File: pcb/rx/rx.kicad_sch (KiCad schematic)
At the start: 2 parts, among them U1 MCP33151-05-E/MS, U2 NCS20162DR2G

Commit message: Backup Prototype
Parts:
- removed U1: MCP33151-05-E/MS, custom-lib:MCP33151-05-E_MS, symbol library:MCP33151-05-E/MS
- removed U2: NCS20162DR2G, custom-lib:NCS20162, symbol library:NCS20162DR2G
- added C1: 33nF, Capacitor_THT:C_Disc_D5.0mm_W2.5mm_P5.00mm, symbol Device:C_Small
- added C10, C12, C17, C19, C3, C6: 330pF, Capacitor_THT:C_Disc_D5.0mm_W2.5mm_P5.00mm, symbol Device:C_Small
- added C11, C18, C26, C27, C29, C4: 0.1uF, Capacitor_THT:C_Disc_D5.0mm_W2.5mm_P5.00mm, symbol Device:C_Small
- added C13, C20, C5: 100nF, Capacitor_THT:C_Disc_D5.0mm_W2.5mm_P5.00mm, symbol Device:C_Small
- added C14, C21, C7: 1nF, Capacitor_THT:C_Disc_D5.0mm_W2.5mm_P5.00mm, symbol Device:C_Small
- added C15, C8: 10nF, Capacitor_THT:C_Disc_D5.0mm_W2.5mm_P5.00mm, symbol Device:C_Small
- added C16, C2, C9: 47nF, Capacitor_THT:C_Disc_D5.0mm_W2.5mm_P5.00mm, symbol Device:C_Small
- added C22: 2.2nf, Capacitor_THT:C_Disc_D5.0mm_W2.5mm_P5.00mm, symbol Device:C_Small
- added C23, C24: 2.2nF, Capacitor_THT:C_Disc_D5.0mm_W2.5mm_P5.00mm, symbol Device:C_Small
- added L1: 0.7mH, Connector_PinHeader_2.54mm:PinHeader_1x02_P2.54mm_Vertical, symbol Device:L
- added L3, L4: 2mH, Connector_PinHeader_2.54mm:PinHeader_1x02_P2.54mm_Vertical, symbol Device:L
- added R1, R2: 10K, Resistor_THT:R_Axial_DIN0207_L6.3mm_D2.5mm_P7.62mm_Horizontal, symbol Device:R_US
- added R10, R13, R15, R3, R5, R8: 750, Resistor_THT:R_Axial_DIN0207_L6.3mm_D2.5mm_P7.62mm_Horizontal, symbol Device:R_US
- added R11, R14, R16, R4, R6, R9: 6.8K, Resistor_THT:R_Axial_DIN0207_L6.3mm_D2.5mm_P7.62mm_Horizontal, symbol Device:R_US
- added R12, R17, R7: 2.2K, Resistor_THT:R_Axial_DIN0207_L6.3mm_D2.5mm_P7.62mm_Horizontal, symbol Device:R_US
- added U1: nice_nano, nice nano:nice_nano, symbol nice_nano:nice_nano
- added U2: MPU-6500, Library:MPU-6500, symbol library:MPU-6500
- added U3: QMC5883P, Library:QMC5883P, symbol library:QMC5883P
- added U4, U5: MCP6004, Library:MCP6004, symbol Amplifier_Operational:MCP6004
- added U6: 74HC4051, Library:74HC4051, symbol 74xx:74HC4051
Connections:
- new net: C19.1, R15.1, R16.2, U4.9 (-)
- new net: C18.2, R15.2
- new net: C15.1, C24.1, L4.1, U4.12 (+)
- new net: C17.1, R13.1, R14.2, U4.13 (-)
- new net: C5.2, C6.2, R6.1, U4.7
- new net: C12.2, C13.2, R11.1, U5.7
- new net: C12.1, R10.1, R11.2, U5.6 (-)
- new net: C2.1, R3.2
- new net: C29.2, R1.1, R2.2, U5.10 (+)
- new net: C10.1, R8.1, R9.2, U5.2 (-)
- new net: C9.1, R8.2
- new net: C19.2, C20.2, R16.1, U4.8
- new net: C11.2, R10.2
- new net: C16.1, R13.2
- new net: C23.1, C8.1, L3.1, U5.3 (+)
- new net: C3.1, R3.1, R4.2, U4.2 (-)
- new net: C4.2, R5.2
- new net: C1.1, C22.1, L1.1, U4.3 (+)
- new net: C6.1, R5.1, R6.2, U4.6 (-)
- new net +3.3V: C26.2, C27.1, R2.1, U1.21 (VCC), U2.13 (VDD), U3.2 (VDD), U4.4 (V+), U5.4 (V+), U6.16 (VCC)
- new net ADC_0: U1.18 (AIN0/P0.02), U5.13 (-), U5.14
- new net ADC_BUFFER: U5.12 (+), U6.3 (A)
- new net GND: C26.1, C27.2, C29.1, R1.2, U1.3 (GND), U1.4 (GND), U2.18 (GND), U3.9 (GND), U4.11 (V-), U5.11 (V-), U6.2 (A6), U6.4 (A7), U6.6 (~{E}), U6.7 (VEE), U6.8 (GND)
- new net SCK: U1.6 (P0.20), U2.23 (SCL/SCLK), U3.1 (SCK)
- new net SDA: U1.5 (P0.17), U2.24 (SDA/SDI), U3.16 (SDA)
- new net SELECT_0: U1.15 (P1.11), U6.11 (S0)
- new net SELECT_1: U1.14 (NFC2/P0.10), U6.10 (S1)
- new net SELECT_2: U1.13 (NFC1/P0.09), U6.9 (S2)
- new net V_BIAS: C1.2, C11.1, C14.1, C15.2, C16.2, C18.1, C2.2, C21.1, C22.2, C23.2, C24.2, C4.1, C7.1, C8.2, C9.2, L1.2, L3.2, L4.2, R12.2, R17.2, R7.2, U5.8, U5.9 (-)
- new net V_OUT1: C17.2, R14.1, U4.10 (+), U4.14, U6.14 (A1)
- new net V_OUT2: C20.1, C21.2, R17.1, U6.13 (A0)
- new net V_OUT3: C3.2, R4.1, U4.1, U4.5 (+), U6.12 (A3)
- new net V_OUT4: C5.1, C7.2, R7.1, U6.15 (A2)
- new net V_OUT5: C10.2, R9.1, U5.1, U5.5 (+), U6.1 (A4)
- new net V_OUT6: C13.1, C14.2, R12.1, U6.5 (A5)
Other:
- note added: "Additionally C4 should be 0.47uF, changed for this specific prototype because I dont have capcitors"
- note added: "R3 should be 51, check research paper"
- note added: "R5 should be 51, but MCP6004 limited to 1MHZ replace when using better op amp"
- note added: "analog digital front end"
- note added: "stage 1 uses negative feedback to amplify 32khz signal using differentiator circuit to amplifer oscilations"
- note added: "unity gain amplifer used to isolate vbias"

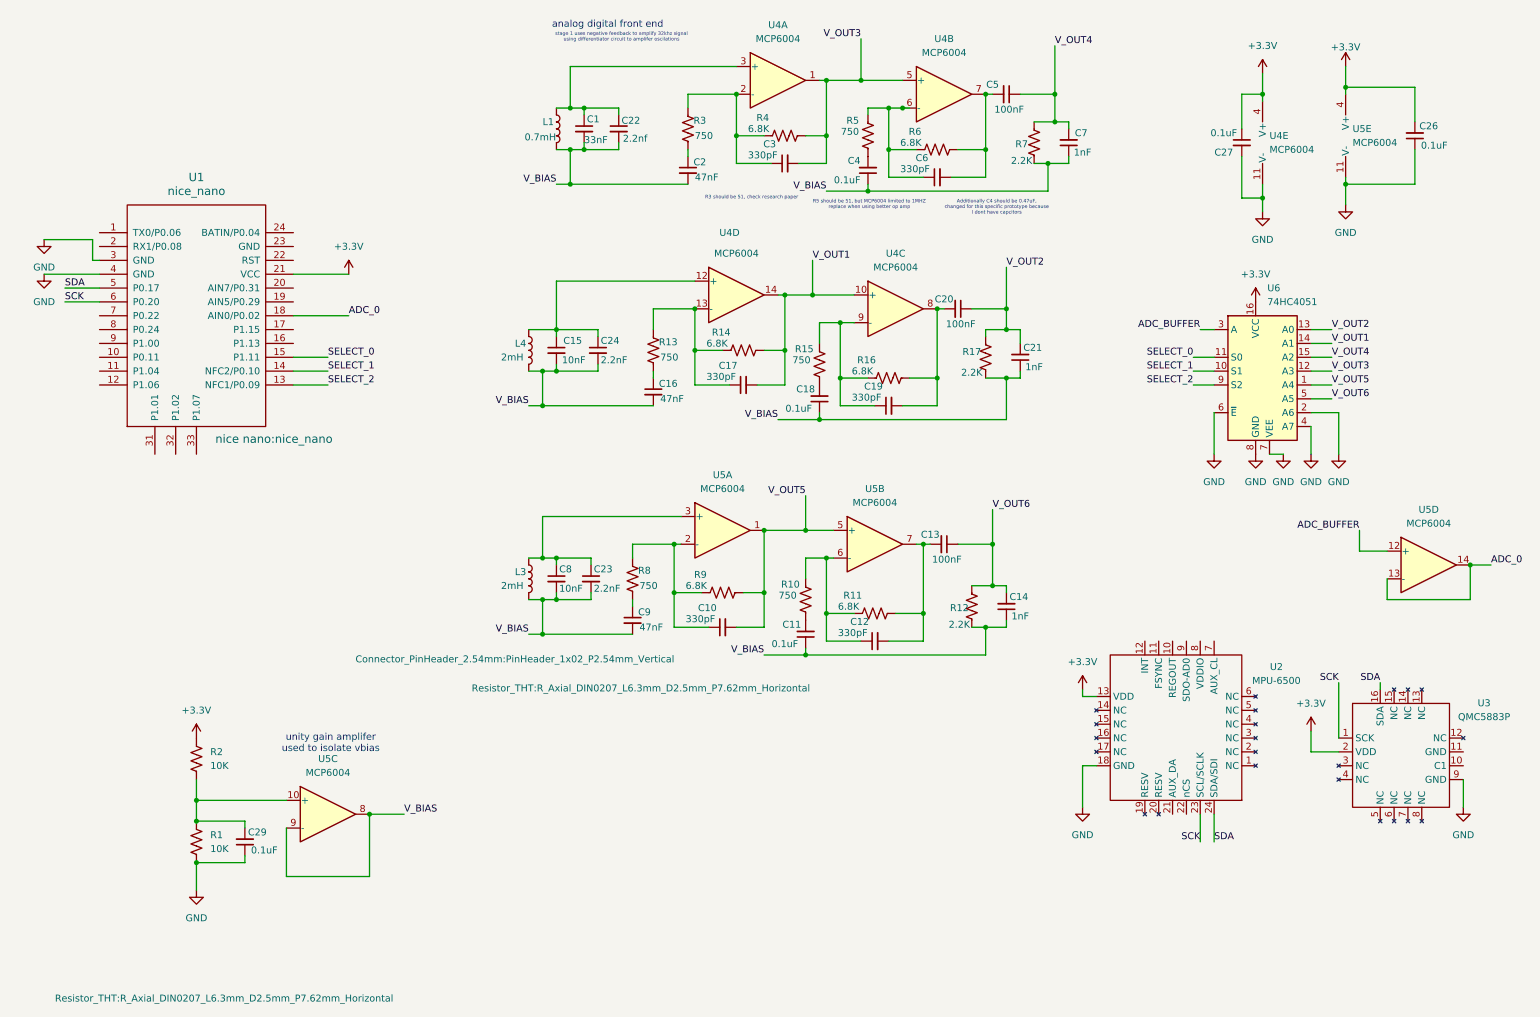
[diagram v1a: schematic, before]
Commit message: Created rx board for order
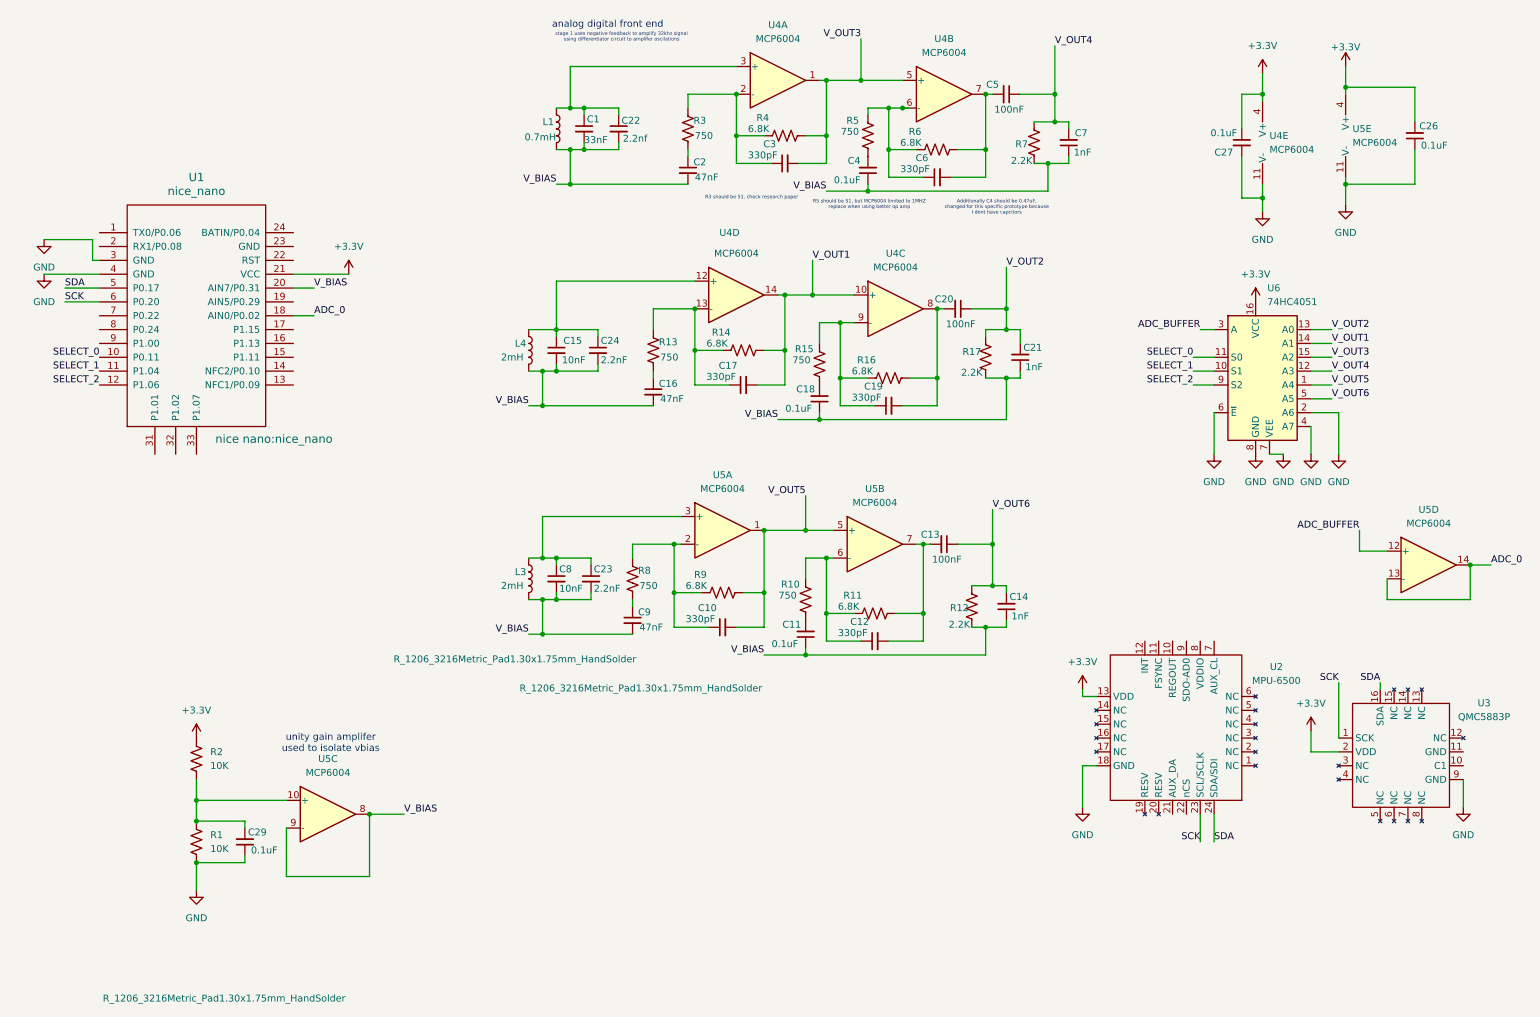
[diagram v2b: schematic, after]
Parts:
- C1, C10, C11, C12, C13, C14, C15, C16, C17, C18, C19, C2, C20, C21, C22, C23, C24, C26, C27, C29, C3, C4, C5, C6, C7, C8, C9: footprint Capacitor_THT:C_Disc_D5.0mm_W2.5mm_P5.00mm -> C_1206_3216Metric_Pad1.33x1.80mm_HandSolder
- L1, L3, L4: footprint Connector_PinHeader_2.54mm:PinHeader_1x02_P2.54mm_Vertical -> R_1206_3216Metric_Pad1.30x1.75mm_HandSolder
- R1, R10, R11, R12, R13, R14, R15, R16, R17, R2, R3, R4, R5, R6, R7, R8, R9: footprint Resistor_THT:R_Axial_DIN0207_L6.3mm_D2.5mm_P7.62mm_Horizontal -> R_1206_3216Metric_Pad1.30x1.75mm_HandSolder
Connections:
- net SELECT_0: now also U1.10 (P0.11); no longer U1.15 (P1.11)
- net SELECT_1: now also U1.11 (P1.04); no longer U1.14 (NFC2/P0.10)
- net SELECT_2: now also U1.12 (P1.06); no longer U1.13 (NFC1/P0.09)
- net V_BIAS: now also U1.20 (AIN7/P0.31)
- net V_OUT3: now also U6.15 (A2); no longer U6.12 (A3)
- net V_OUT4: now also U6.12 (A3); no longer U6.15 (A2)

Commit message: Finished Rx
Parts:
- added BT1: Battery, JST_PH_B2B-PH-K_1x02_P2.00mm_Vertical, symbol Device:Battery
- added SW1: SW_SPDT, Library:EG1218, symbol Switch:SW_SPDT
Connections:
- new net: BT1.1 (+), SW1.2 (B)
- new net B+: SW1.1 (A), U1.34 (BATIN/P0.04)
- new net B-: BT1.2 (-), U1.30 (GND)
- no-connect marks 0 -> 27

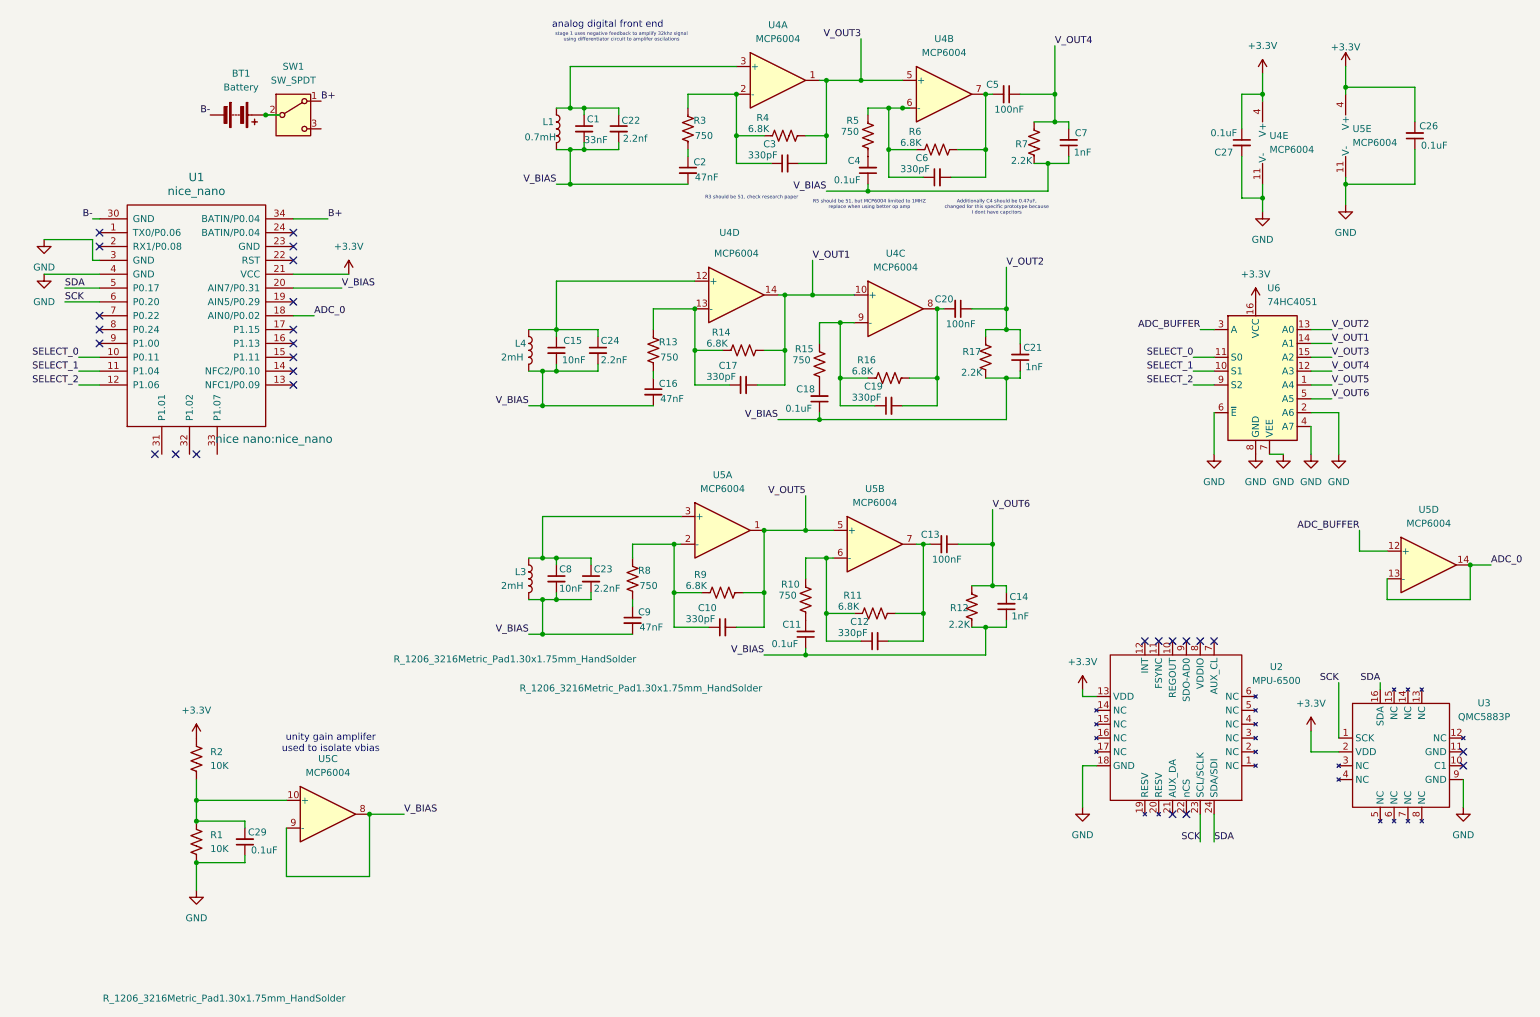
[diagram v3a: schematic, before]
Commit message: Update Rx board to include anchor
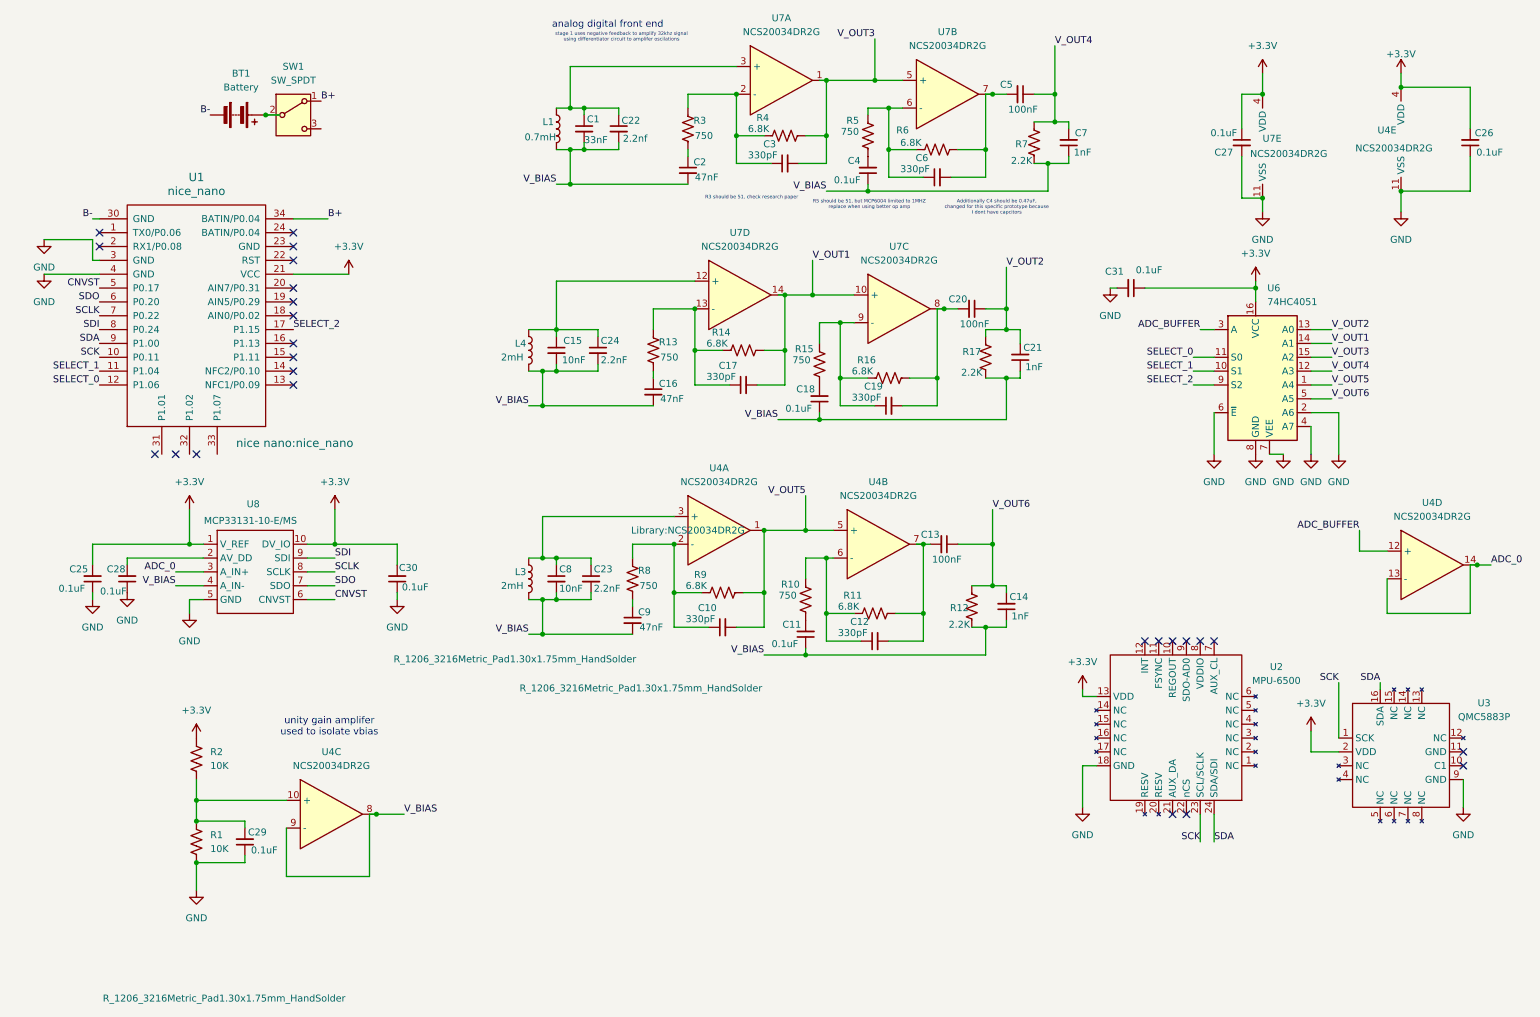
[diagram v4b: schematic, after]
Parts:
- removed U4, U5: MCP6004, Library:MCP6004, symbol Amplifier_Operational:MCP6004
- added C25, C28, C30, C31: 0.1uF, C_1206_3216Metric_Pad1.33x1.80mm_HandSolder, symbol Device:C_Small
- added U4, U7: NCS20034DR2G, Library:NCS20034DR2G, symbol library:NCS20034DR2G
- added U8: MCP33131-10-E/MS, Library:MCP33131, symbol library:MCP33131-10-E/MS
- U6: footprint Library:74HC4051 -> Library:74HC4051-chip
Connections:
- net +3.3V: now also C25.2, C30.2, C31.1, U4.4 (VDD), U7.4 (VDD), U8.1 (V_REF), U8.10 (DV_IO)
- net ADC_0: now also U4.13 (-), U4.14, U8.3 (A_IN+); no longer U1.18 (AIN0/P0.02)
- net ADC_BUFFER: now also U4.12 (+)
- net GND: now also C25.1, C28.1, C30.1, C31.2, U4.11 (VSS), U7.11 (VSS), U8.5 (GND)
- net SCK: now also U1.10 (P0.11); no longer U1.6 (P0.20)
- net SDA: now also U1.9 (P1.00); no longer U1.5 (P0.17)
- net SELECT_0: now also U1.12 (P1.06); no longer U1.10 (P0.11)
- net SELECT_2: now also U1.17 (P1.15); no longer U1.12 (P1.06)
- net V_BIAS: now also U4.8, U4.9 (-), U8.4 (A_IN-); no longer U1.20 (AIN7/P0.31)
- net V_OUT1: now also U7.10 (+), U7.14
- net V_OUT3: now also U7.1, U7.5 (+)
- net V_OUT5: now also U4.1, U4.5 (+)
- net at C19.1, R15.1, R16.2: now also U7.9 (-)
- net at C15.1, C24.1, L4.1: now also U7.12 (+)
- net at C17.1, R13.1, R14.2: now also U7.13 (-)
- net at C5.2, C6.2, R6.1: now also U7.7
- net at C12.2, C13.2, R11.1: now also U4.7
- net at C12.1, R10.1, R11.2: now also U4.6 (-)
- net at C29.2, R1.1, R2.2: now also U4.10 (+)
- net at C10.1, R8.1, R9.2: now also U4.2 (-)
- net at C19.2, C20.2, R16.1: now also U7.8
- net SCLK: now reaches U1.7 (P0.22)
- net SCLK: now also U8.8 (SCLK)
- net SDI: now reaches U1.8 (P0.24)
- net SDI: now also U8.9 (SDI)
- net at C23.1, C8.1, L3.1: now also U4.3 (+)
- net at C3.1, R3.1, R4.2: now also U7.2 (-)
- net at C1.1, C22.1, L1.1: now also U7.3 (+)
- net at C6.1, R5.1, R6.2: now also U7.6 (-)
- new net: C28.2, U8.2 (AV_DD)
- new net CNVST: U1.5 (P0.17), U8.6 (CNVST)
- new net SDO: U1.6 (P0.20), U8.7 (SDO)
- no-connect marks 27 -> 25
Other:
- moved on the sheet: C20, C26, C5

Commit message: Update
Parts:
- C11, C18, C4: value 0.1uF -> 0.47uF
- R10, R15, R5: value 750 -> 51
- R13, R3, R8: value 750 -> 510
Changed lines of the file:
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@@
 			)
 		)
-		(property "Value" "750"
+		(property "Value" "51"
 			(at 154.178 76.708 0)
 			(show_name no)
@@
 			)
 		)
-		(property "Value" "750"
+		(property "Value" "510"
 			(at 124.46 118.11 0)
 			(show_name no)
@@
 			)
 		)
-		(property "Value" "750"
+		(property "Value" "51"
 			(at 151.638 119.888 0)
 			(show_name no)
@@
 			)
 		)
-		(property "Value" "0.1uF"
+		(property "Value" "0.47uF"
 			(at 151.13 128.778 0)
 			(show_name no)
@@
 			)
 		)
-		(property "Value" "0.1uF"
+		(property "Value" "0.47uF"
 			(at 162.56 43.688 0)
 			(show_name no)
@@
 			)
 		)
-		(property "Value" "750"
+		(property "Value" "510"
 			(at 134.62 35.56 0)
 			(show_name no)
@@
 			)
 		)
-		(property "Value" "0.1uF"
+		(property "Value" "0.47uF"
 			(at 153.67 85.598 0)
 			(show_name no)
@@
 			)
 		)
-		(property "Value" "750"
+		(property "Value" "510"
 			(at 128.27 76.2 0)
 			(show_name no)
@@
 			)
 		)
-		(property "Value" "750"
+		(property "Value" "51"
 			(at 163.068 34.798 0)
 			(show_name no)
